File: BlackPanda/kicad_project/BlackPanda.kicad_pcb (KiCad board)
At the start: 4 copper layers, 47.5 x 41.7 mm, 86 parts, among them P1 TYPE-C-31-M-04, Q1 DDTA143ECA-7-F P08, Q2 DDTA143ECA-7-F P08, Q3 PDTC114EU, Q4 HY12P03C2, SW1 SW_Push, U1 AP22615AWU-7, U10 TJA1042TK-3, U11 TJA1042TK-3, U12 XL1509-3.3, U2 SiP32431DR3, U3 10_0_QHHTZB6_3, U4 NEO-M8M, U5 FM-B1921RGBA-SH, U6 TPS5450DDAR, U7 STM32F413RGTx, U8 TJA1042TK-3, U9 TJA1042TK-3, Y1 X322516MLB4SI

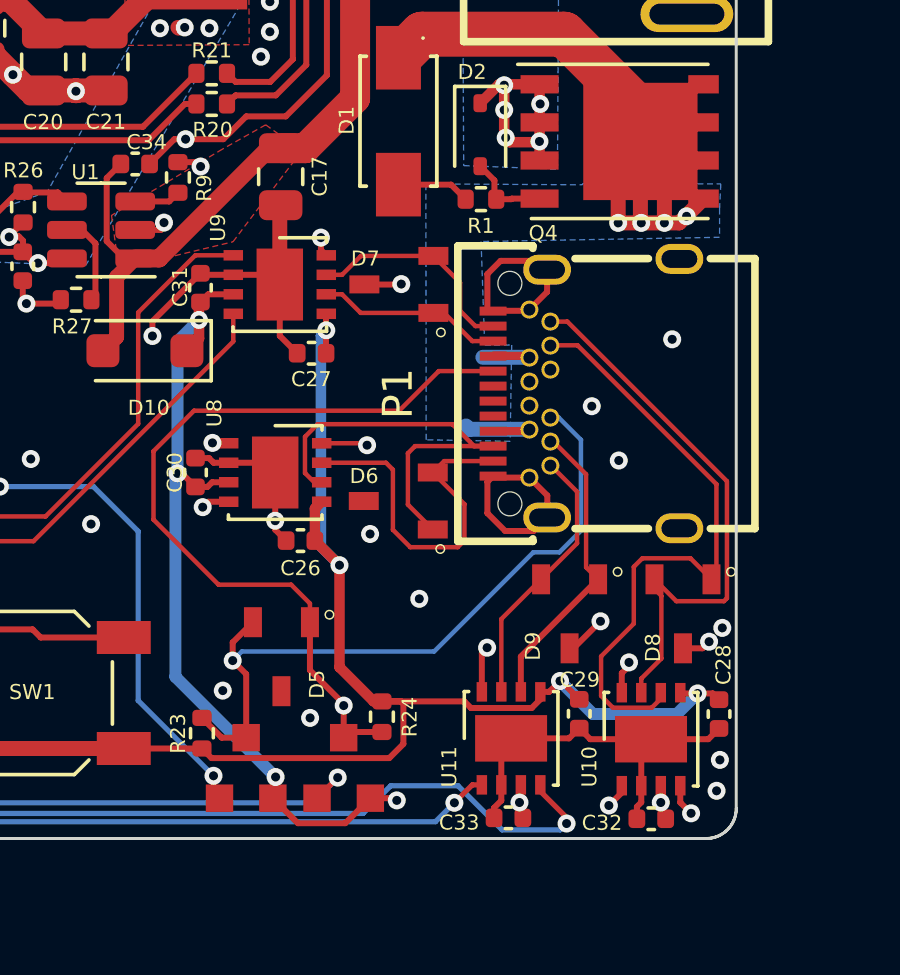
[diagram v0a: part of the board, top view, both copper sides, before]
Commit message: TJA1042 uses HVSON8
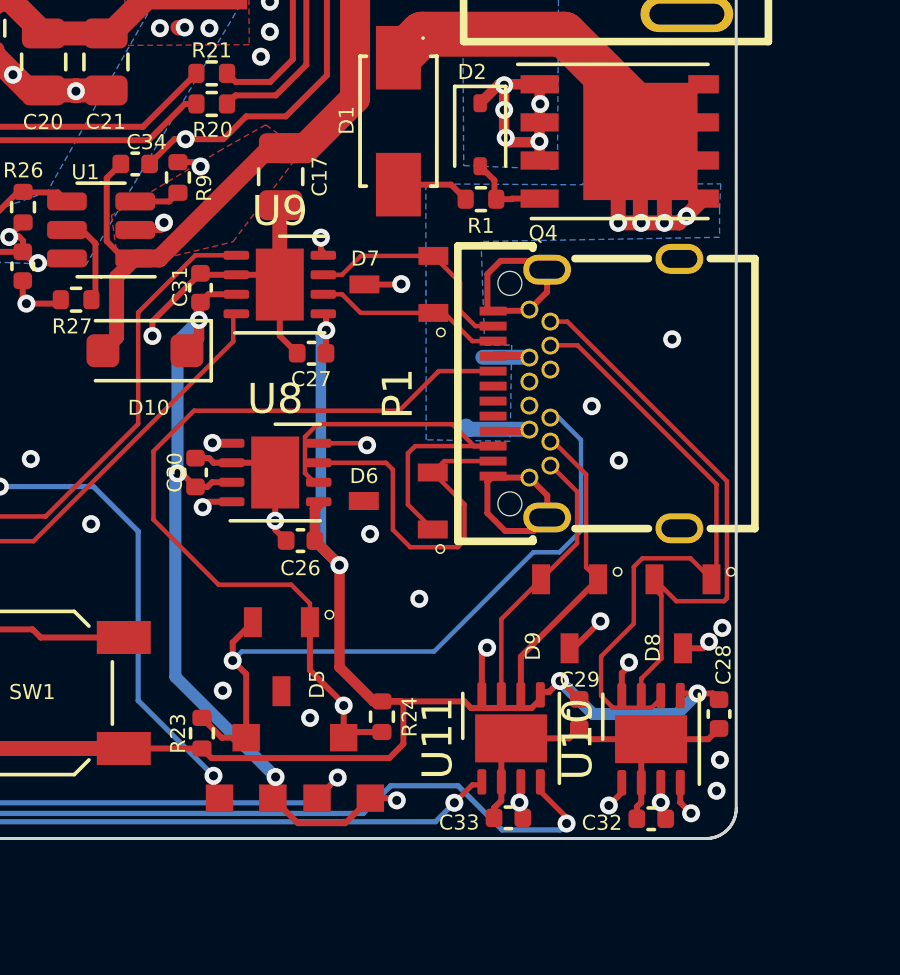
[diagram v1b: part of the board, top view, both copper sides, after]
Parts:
- U10, U11, U8, U9: footprint Package_DFN_QFN:DFN-8-1EP_3x3mm_P0.65mm_EP1.55x2.4mm -> Package_SON:HVSON-8-1EP_3x3mm_P0.65mm_EP1.6x2.4mm
